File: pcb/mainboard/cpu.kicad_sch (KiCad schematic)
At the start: 48 parts, among them U101 MCIMX7S5EVM08SC, Y101 24MHz, Y102 32.768kHz

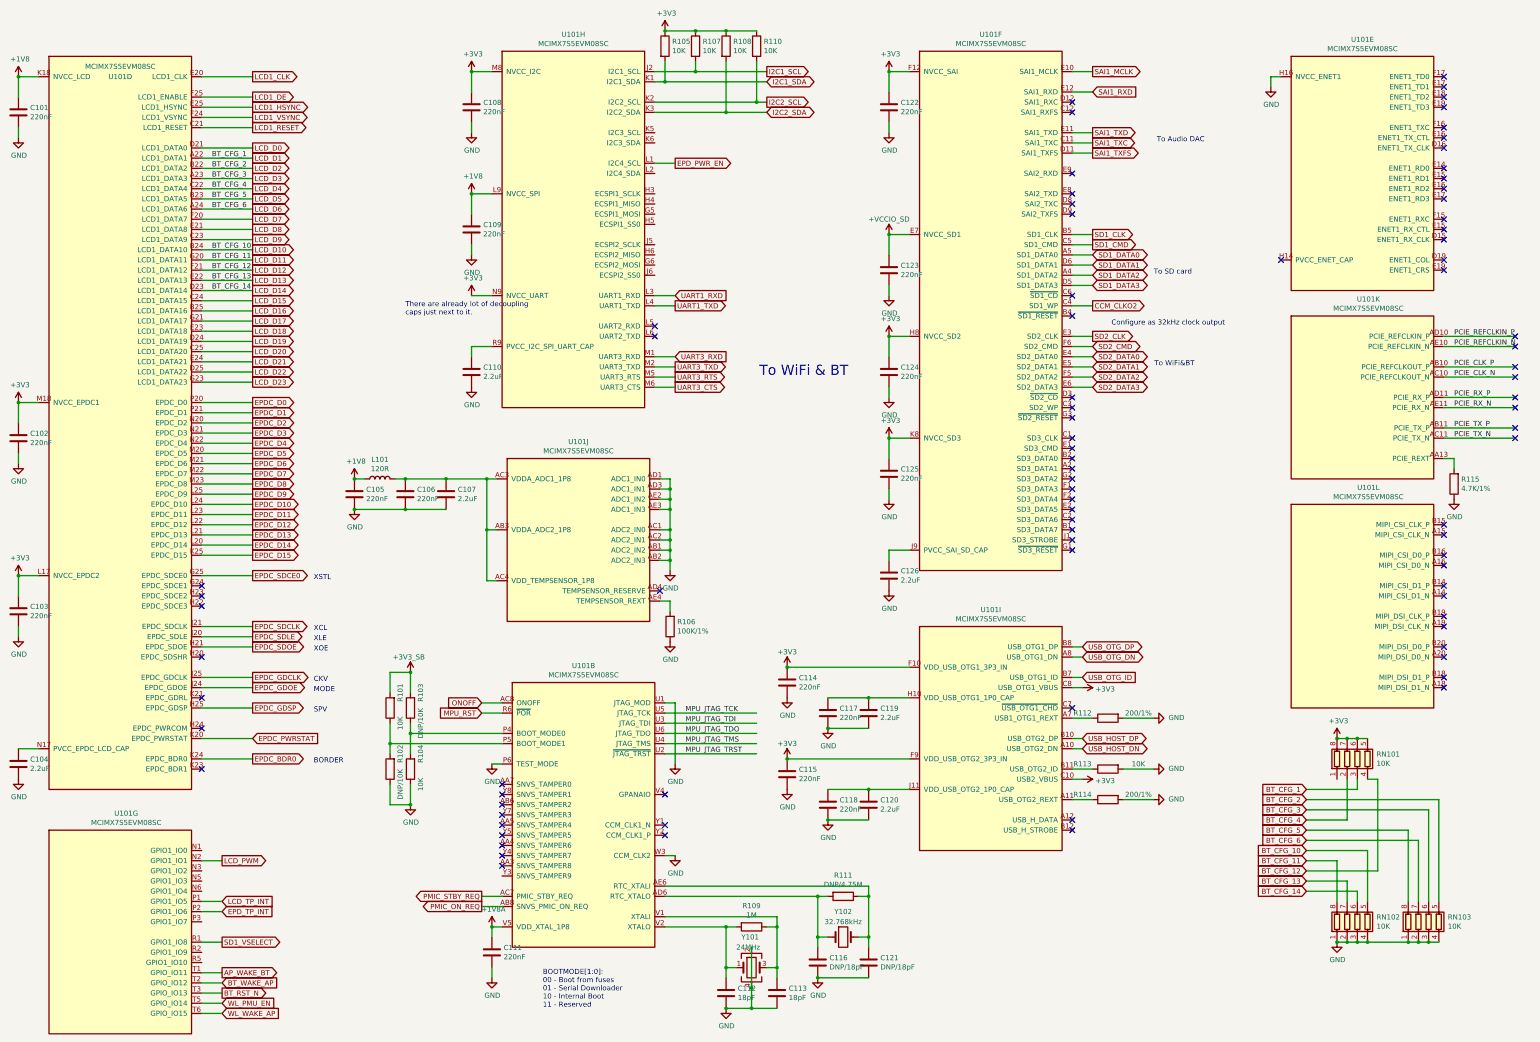
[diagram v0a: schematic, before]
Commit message: pcb: preliminary r0p1 schematics
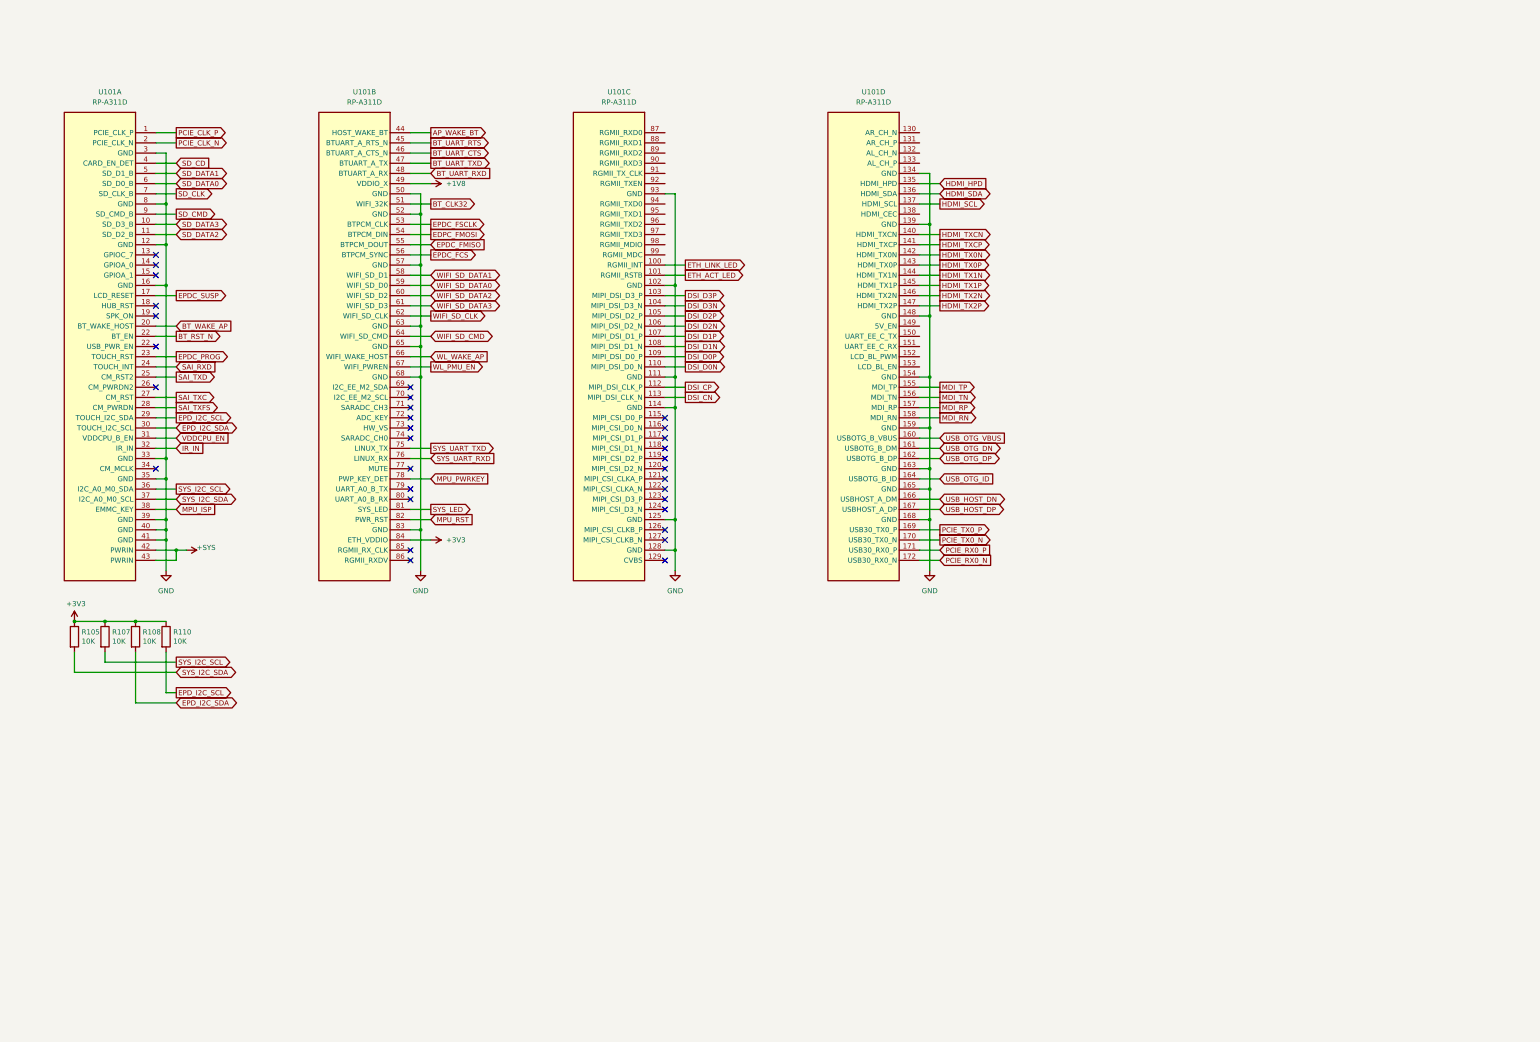
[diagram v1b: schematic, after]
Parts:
- removed C101, C102, C103, C105, C106, C108, C109, C111, C114, C115, C117, C118, C122, C123, C124, C125: 220nF, Capacitor_SMD:C_0402_1005Metric, symbol Device:C
- removed C104, C107, C110, C119, C120, C126: 2.2uF, Capacitor_SMD:C_0402_1005Metric, symbol Device:C
- removed C112, C113: 18pF, Capacitor_SMD:C_0402_1005Metric, symbol Device:C
- removed C116, C121: DNP/18pF, Capacitor_SMD:C_0402_1005Metric, symbol Device:C
- removed L101: 120R, Inductor_SMD:L_0603_1608Metric, symbol Device:L
- removed R101, R104, R113: 10K, Resistor_SMD:R_0402_1005Metric, symbol Device:R
- removed R102, R103: DNP/10K, Resistor_SMD:R_0402_1005Metric, symbol Device:R
- removed R106: 100K/1%, Resistor_SMD:R_0402_1005Metric, symbol Device:R
- removed R109: 1M, Resistor_SMD:R_0402_1005Metric, symbol Device:R
- removed R111: DNP/4.75M, Resistor_SMD:R_0402_1005Metric, symbol Device:R
- removed R112, R114: 200/1%, Resistor_SMD:R_0402_1005Metric, symbol Device:R
- removed R115: 4.7K/1%, Resistor_SMD:R_0402_1005Metric, symbol Device:R
- removed RN101, RN102, RN103: 10K, Resistor_SMD:R_Array_Convex_4x0402, symbol Device:R_Pack04
- removed U101: MCIMX7S5EVM08SC, footprints:BGA-541_25x25_19.0x19.0mm, symbol symbols:MCIMX7S5EVM08SC
- removed Y101: 24MHz, Oscillator:Oscillator_SMD_Abracon_ASE-4Pin_3.2x2.5mm, symbol Device:Crystal_GND24
- removed Y102: 32.768kHz, Crystal:Crystal_SMD_TXC_9HT11-2Pin_2.0x1.2mm_HandSoldering, symbol Device:Crystal
- added U101: RP-A311D, footprints:RP-A311D, symbol symbols:RP-A311D
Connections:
- net +1V8: now also U101.49 (VDDIO_X)
- net +3V3: now also U101.84 (ETH_VDDIO)
- net AP_WAKE_BT: now also U101.44 (HOST_WAKE_BT)
- net BT_RST_N: now also U101.22 (USB_PWR_EN)
- net BT_WAKE_AP: now also U101.20 (BT_WAKE_HOST)
- net GND: now also U101.102 (GND), U101.111 (GND), U101.114 (GND), U101.12 (GND), U101.125 (GND), U101.128 (GND), U101.134 (GND), U101.139 (GND), U101.148 (GND), U101.154 (GND), U101.159 (GND), U101.16 (GND), U101.163 (GND), U101.165 (GND), U101.168 (GND), U101.3 (GND), U101.33 (GND), U101.35 (GND), U101.39 (GND), U101.40 (GND), U101.41 (GND), U101.50 (GND), U101.52 (GND), U101.57 (GND), U101.63 (GND), U101.65 (GND), U101.68 (GND), U101.8 (GND), U101.83 (GND), U101.93 (GND)
- net MPU_RST: now also U101.82 (PWR_RST)
- net PCIE_CLK_N: now also U101.2 (PCIE_CLK_N)
- net PCIE_CLK_P: now also U101.1 (PCIE_CLK_P)
- net USB_HOST_DN: now also U101.166 (USBHOST_A_DM)
- net USB_HOST_DP: now also U101.167 (USBHOST_A_DP)
- net USB_OTG_DN: now also U101.161 (USBOTG_B_DM)
- net USB_OTG_DP: now also U101.162 (USBOTG_B_DP)
- net USB_OTG_ID: now also U101.164 (USBOTG_B_ID)
- net WL_PMU_EN: now also U101.67 (WIFI_PWREN)
- net WL_WAKE_AP: now also U101.66 (WIFI_WAKE_HOST)
- net I2C1_SCL renamed SYS_I2C_SCL
- net SYS_I2C_SCL: now also U101.36 (I2C_A0_M0_SDA)
- net I2C1_SDA renamed SYS_I2C_SDA
- net SYS_I2C_SDA: now also U101.37 (I2C_A0_M0_SCL)
- net I2C2_SCL renamed EPD_I2C_SCL
- net EPD_I2C_SCL: now also U101.29 (TOUCH_I2C_SDA)
- net I2C2_SDA renamed EPD_I2C_SDA
- net EPD_I2C_SDA: now also U101.30 (TOUCH_I2C_SCL)
- new net +SYS: U101.42 (PWRIN), U101.43 (PWRIN)
- new net BT_CLK32: U101.51 (WIFI_32K)
- new net BT_UART_CTS: U101.46 (BTUART_A_CTS_N)
- new net BT_UART_RTS: U101.45 (BTUART_A_RTS_N)
- new net BT_UART_RXD: U101.48 (BTUART_A_RX)
- new net BT_UART_TXD: U101.47 (BTUART_A_TX)
- new net DSI_CN: U101.113 (MIPI_DSI_CLK_N)
- new net DSI_CP: U101.112 (MIPI_DSI_CLK_P)
- new net DSI_D0N: U101.110 (MIPI_DSI_D0_N)
- new net DSI_D0P: U101.109 (MIPI_DSI_D0_P)
- new net DSI_D1N: U101.108 (MIPI_DSI_D1_N)
- new net DSI_D1P: U101.107 (MIPI_DSI_D1_P)
- new net DSI_D2N: U101.106 (MIPI_DSI_D2_N)
- new net DSI_D2P: U101.105 (MIPI_DSI_D2_P)
- new net DSI_D3N: U101.104 (MIPI_DSI_D3_N)
- new net DSI_D3P: U101.103 (MIPI_DSI_D3_P)
- new net EDPC_FMOSI: U101.54 (BTPCM_DIN)
- new net EPDC_FCS: U101.56 (BTPCM_SYNC)
- new net EPDC_FMISO: U101.55 (BTPCM_DOUT)
- new net EPDC_FSCLK: U101.53 (BTPCM_CLK)
- new net EPDC_PROG: U101.23 (TOUCH_RST)
- new net EPDC_SUSP: U101.17 (LCD_RESET)
- new net ETH_ACT_LED: U101.101 (RGMII_RSTB)
- new net ETH_LINK_LED: U101.100 (RGMII_INT)
- new net HDMI_HPD: U101.135 (HDMI_HPD)
- new net HDMI_SCL: U101.137 (HDMI_SCL)
- new net HDMI_SDA: U101.136 (HDMI_SDA)
- new net HDMI_TX0N: U101.142 (HDMI_TX0N)
- new net HDMI_TX0P: U101.143 (HDMI_TX0P)
- new net HDMI_TX1N: U101.144 (HDMI_TX1N)
- new net HDMI_TX1P: U101.145 (HDMI_TX1P)
- new net HDMI_TX2N: U101.146 (HDMI_TX2N)
- new net HDMI_TX2P: U101.147 (HDMI_TX2P)
- new net HDMI_TXCN: U101.140 (HDMI_TXCN)
- new net HDMI_TXCP: U101.141 (HDMI_TXCP)
- new net IR_IN: U101.32 (IR_IN)
- new net MDI_RN: U101.158 (MDI_RN)
- new net MDI_RP: U101.157 (MDI_RP)
- new net MDI_TN: U101.156 (MDI_TN)
- new net MDI_TP: U101.155 (MDI_TP)
- new net MPU_ISP: U101.38 (EMMC_KEY)
- new net MPU_PWRKEY: U101.78 (PWP_KEY_DET)
- new net PCIE_RX0_N: U101.172 (USB30_RX0_N)
- new net PCIE_RX0_P: U101.171 (USB30_RX0_P)
- new net PCIE_TX0_N: U101.170 (USB30_TX0_N)
- new net PCIE_TX0_P: U101.169 (USB30_TX0_P)
- new net SAI_RXD: U101.24 (TOUCH_INT)
- new net SAI_TXC: U101.27 (CM_RST)
- new net SAI_TXD: U101.25 (CM_RST2)
- new net SAI_TXFS: U101.28 (CM_PWRDN)
- new net SD_CD: U101.4 (CARD_EN_DET)
- new net SD_CLK: U101.7 (SD_CLK_B)
- new net SD_CMD: U101.9 (SD_CMD_B)
- new net SD_DATA0: U101.6 (SD_D0_B)
- new net SD_DATA1: U101.5 (SD_D1_B)
- new net SD_DATA2: U101.11 (SD_D2_B)
- new net SD_DATA3: U101.10 (SD_D3_B)
- new net SYS_LED: U101.81 (SYS_LED)
- new net SYS_UART_RXD: U101.76 (LINUX_RX)
- new net SYS_UART_TXD: U101.75 (LINUX_TX)
- new net USB_OTG_VBUS: U101.160 (USBOTG_B_VBUS)
- new net VDDCPU_EN: U101.31 (VDDCPU_B_EN)
- new net WIFI_SD_CLK: U101.62 (WIFI_SD_CLK)
- new net WIFI_SD_CMD: U101.64 (WIFI_SD_CMD)
- new net WIFI_SD_DATA0: U101.59 (WIFI_SD_D0)
- new net WIFI_SD_DATA1: U101.58 (WIFI_SD_D1)
- new net WIFI_SD_DATA2: U101.60 (WIFI_SD_D2)
- new net WIFI_SD_DATA3: U101.61 (WIFI_SD_D3)
- no-connect marks 85 -> 32
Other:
- note removed: "BOOTMODE[1:0]: 00 - Boot from fuses 01 - Serial Downloader 10 - Internal Boot 11 - Reserved"
- note removed: "BORDER"
- note removed: "CKV"
- note removed: "Configure as 32kHz clock output"
- note removed: "MODE"
- note removed: "SPV"
- note removed: "There are already lot of decoupling caps just next to it."
- note removed: "To Audio DAC"
- note removed: "To SD card"
- note removed: "To WiFi & BT"
- note removed: "To WiFi&BT"
- note removed: "XCL"
- note removed: "XLE"
- note removed: "XOE"
- note removed: "XSTL"
- company: Copyright EI-2030 2021. / Engineer: Wenting Zhang -> Copyright Modos 2021. / Engineer: Wenting Zhang
- moved on the sheet: R105, R107, R108, R110

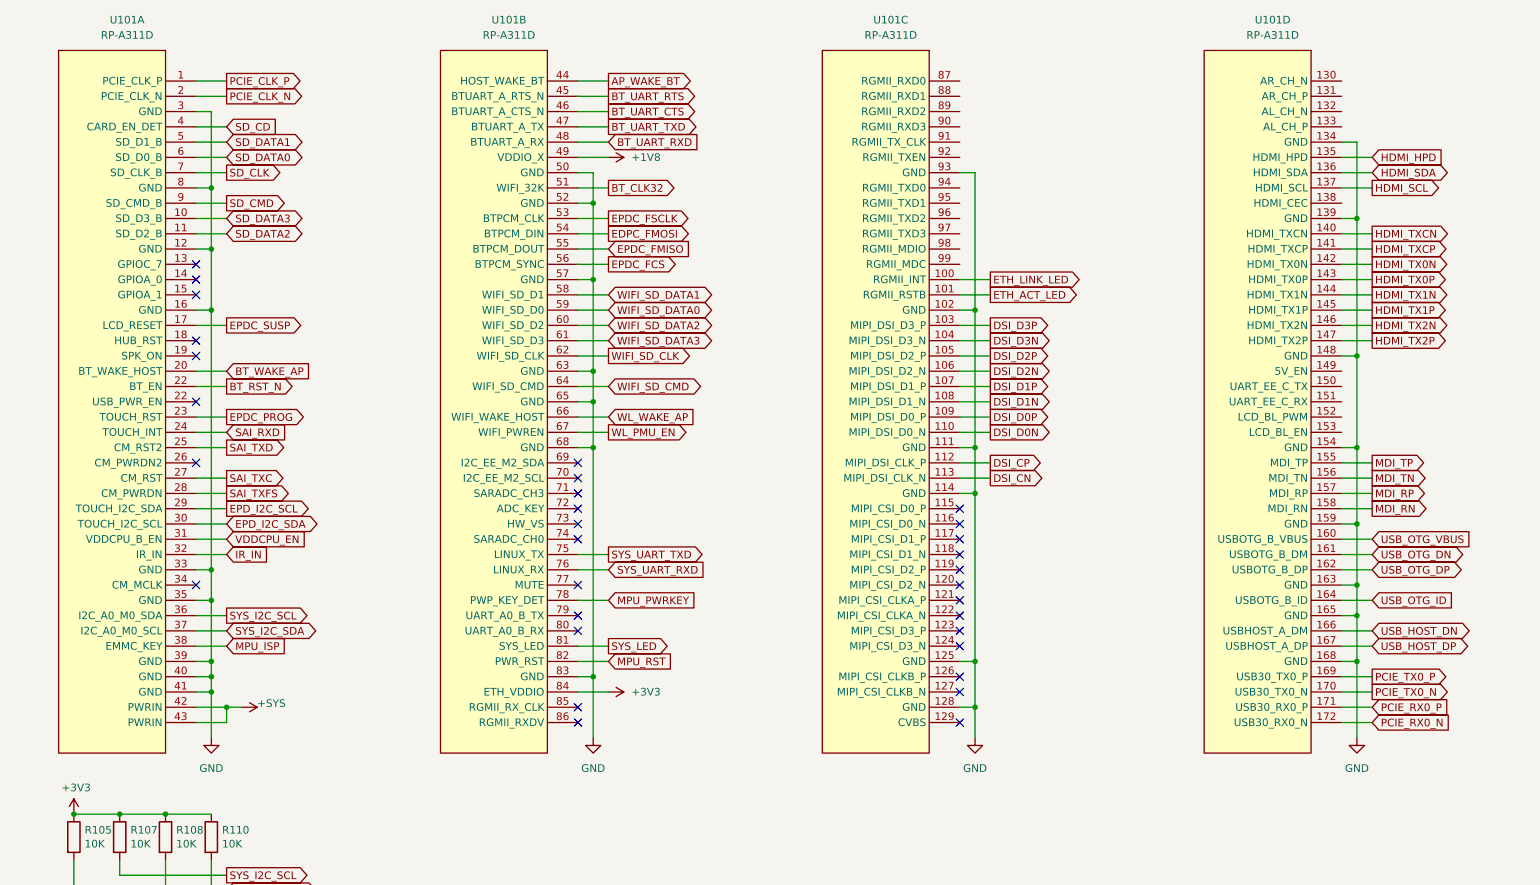
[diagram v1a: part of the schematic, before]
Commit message: pcb: initial placement for mb
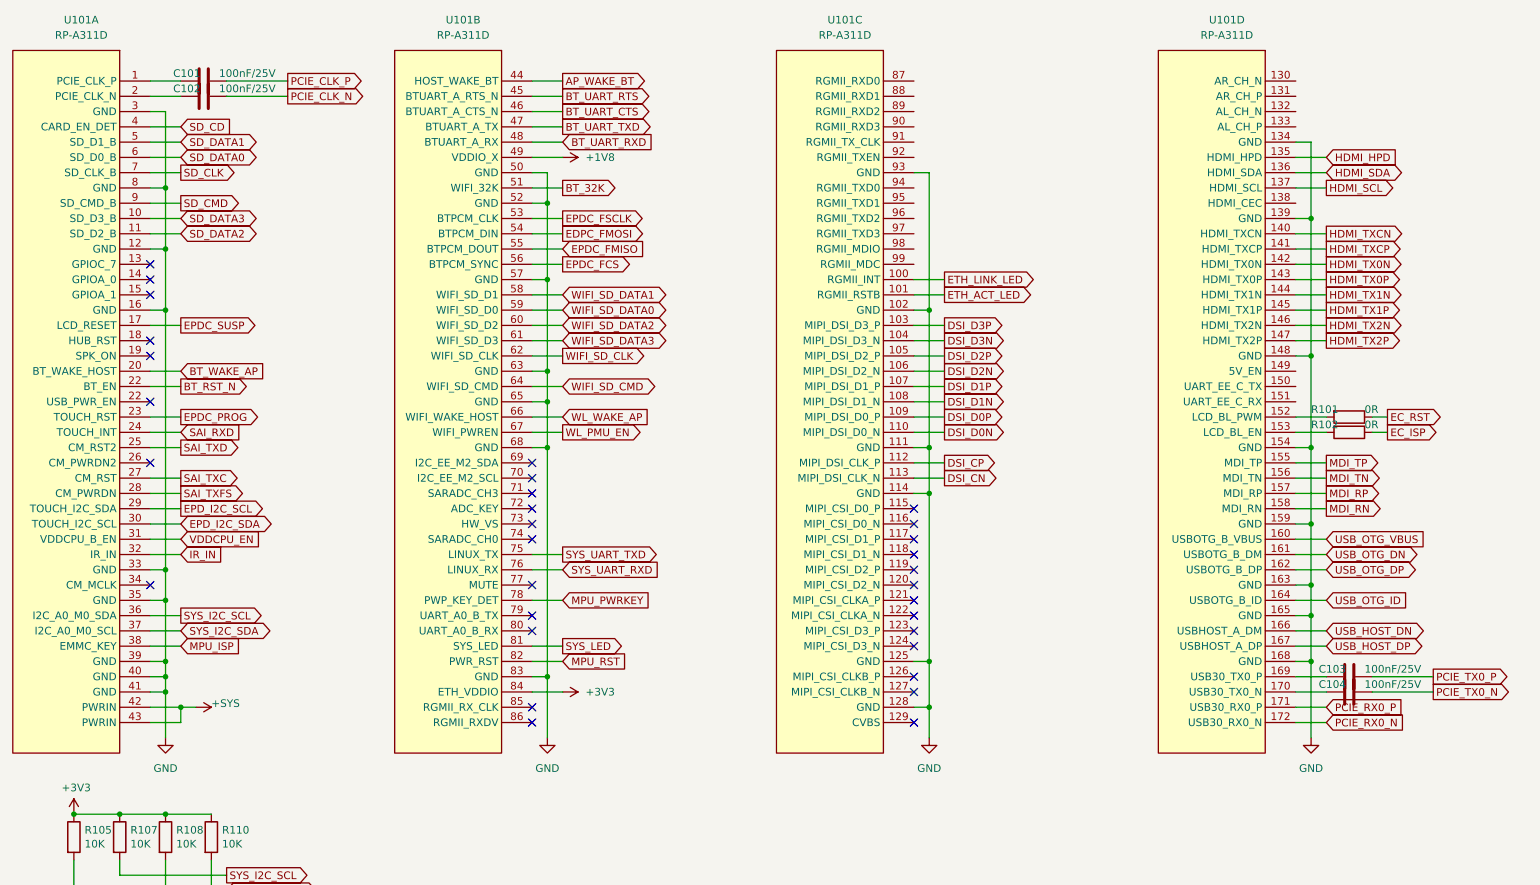
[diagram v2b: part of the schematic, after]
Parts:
- added C101, C102, C103, C104: 100nF/25V, Capacitor_SMD:C_0402_1005Metric, symbol Device:C
- added R101, R102: 0R, Resistor_SMD:R_0402_1005Metric, symbol Device:R
- R105, R107, R108, R110: LCSC (none) -> C60489; Ref.Price (none) -> 0.0006
- U101: Ref.Price (none) -> 88
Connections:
- net PCIE_CLK_N: now also C102.1; no longer U101.2 (PCIE_CLK_N)
- net PCIE_CLK_P: now also C101.1; no longer U101.1 (PCIE_CLK_P)
- net PCIE_TX0_N: now also C104.1; no longer U101.170 (USB30_TX0_N)
- net PCIE_TX0_P: now also C103.1; no longer U101.169 (USB30_TX0_P)
- net at U101.152 (LCD_BL_PWM): now also R101.2
- net at U101.153 (LCD_BL_EN): now also R102.2
- net BT_CLK32 renamed BT_32K
- new net: C104.2, U101.170 (USB30_TX0_N)
- new net: C103.2, U101.169 (USB30_TX0_P)
- new net: C101.2, U101.1 (PCIE_CLK_P)
- new net: C102.2, U101.2 (PCIE_CLK_N)
- new net EC_ISP: R102.1
- new net EC_RST: R101.1
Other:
- moved on the sheet: U101A, U101B, U101C, U101D

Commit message: pcb: r0.1 mb routing done
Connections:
- net PCIE_PERST: now reaches U101.87 (RGMII_RXD0)
- net EDPC_FMOSI renamed EPDC_FMOSI
- net EPDC_FSCLK renamed EPDC_FCCLK
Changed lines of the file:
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@@
+    (stroke (width 0) (type default) (color 0 0 0 0))
+  )
+  (wire (pts (xy 180.34 45.72) (xy 185.42 45.72))
     (stroke (width 0) (type default) (color 0 0 0 0))
   )
@@
     )
   )
-  (global_label "EPDC_FSCLK" (shape output) (at 121.92 68.58 0) (fields_autoplaced)
-    (effects (font (size 1.27 1.27)) (justify left))
-    (property "Intersheet References" "${INTERSHEET_REFS}" (id 0) (at 136.126 68.5006 0)
-      (effects (font (size 1.27 1.27)) (justify left) hide)
-    )
-  )
-  (global_label "EDPC_FMOSI" (shape output) (at 121.92 71.12 0) (fields_autoplaced)
+  (global_label "EPDC_FCCLK" (shape output) (at 121.92 68.58 0) (fields_autoplaced)
+    (effects (font (size 1.27 1.27)) (justify left))
+    (property "Intersheet References" "${INTERSHEET_REFS}" (id 0) (at 136.1864 68.5006 0)
+      (effects (font (size 1.27 1.27)) (justify left) hide)
+    )
+  )
+  (global_label "EPDC_FMOSI" (shape output) (at 121.92 71.12 0) (fields_autoplaced)
     (effects (font (size 1.27 1.27)) (justify left))
     (property "Intersheet References" "${INTERSHEET_REFS}" (id 0) (at 135.9445 71.0406 0)
@@
       (effects (font (size 1.27 1.27)) (justify left) hide)
     )
+  )
+  (global_label "PCIE_PERST" (shape output) (at 185.42 45.72 0) (fields_autoplaced)
+    (effects (font (size 1.27 1.27)) (justify left))
+    (property "Intersheet References" "${INTERSHEET_REFS}" (id 0) (at 198.9607 45.6406 0)
+      (effects (font (size 1.27 1.27)) (justify left) hide)
+    )
